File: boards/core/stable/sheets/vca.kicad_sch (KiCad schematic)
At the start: 23 parts, among them Q202 BC847BS, U207 TL072

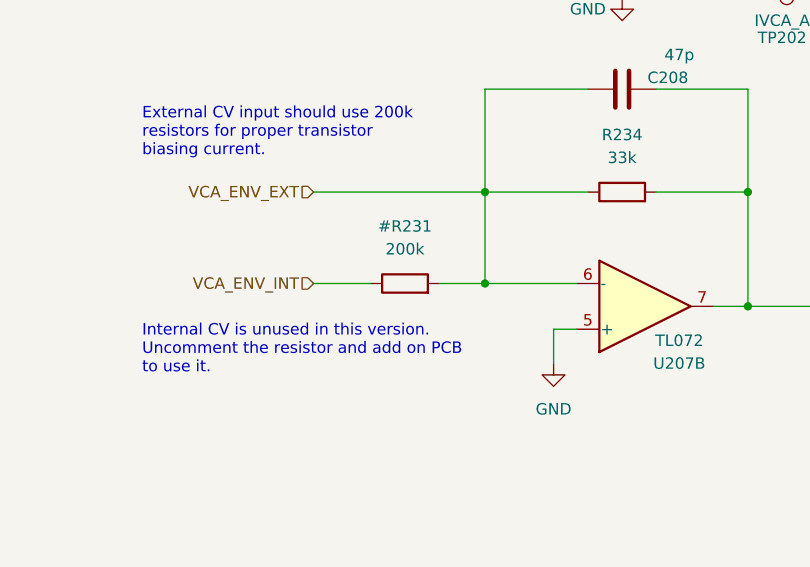
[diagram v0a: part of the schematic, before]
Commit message: Updated and checked Core board BOM
ref https://github.com/shmoergh/hog/issues/19
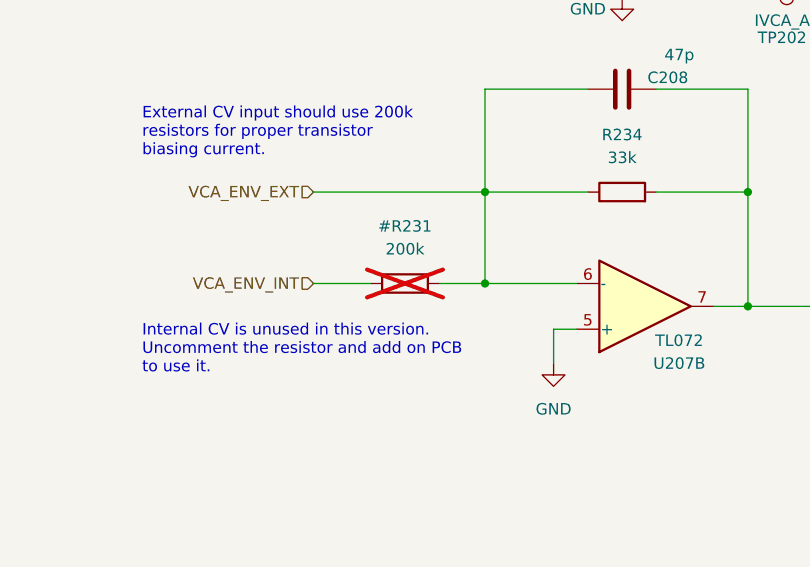
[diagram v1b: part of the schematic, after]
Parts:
- #R231: now not fitted; now left out of the parts list
- C206, C207, C208, R201, R234, R238, R239, R56, R58, R59, U207: Vendor (none) -> JLCPCB
- Q202: LCSC C699265 -> C5380687; Vendor (none) -> JLCPCB
- R54: LCSC (none) -> JLCPCB

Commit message: Added JLCPCB production files to Core
ref https://github.com/shmoergh/hog/issues/19
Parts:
- R54: Field4 C22962 -> (none); LCSC JLCPCB -> C22962; Vendor (none) -> JLCPCB
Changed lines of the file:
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@@
 			)
 		)
-		(property "Field4" "C22962"
+		(property "LCSC" "C22962"
 			(at 130.81 93.98 0)
 			(effects
@@
 			)
 		)
-		(property "Vendor" ""
+		(property "Vendor" "JLCPCB"
 			(at 130.81 93.98 0)
 			(effects
-				(font
-					(size 1.27 1.27)
-				)
-				(hide yes)
-			)
-		)
-		(property "LCSC" "JLCPCB"
-			(at 130.81 93.98 0)
-			(effects

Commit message: Replaced VCA dual BJT footprint
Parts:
- Q202: footprint Package_TO_SOT_SMD:SOT-363_SC-70-6 -> Package_TO_SOT_SMD:SOT-363_SC-70-6_Handsoldering
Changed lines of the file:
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@@
 			)
 		)
-		(property "Footprint" "Package_TO_SOT_SMD:SOT-363_SC-70-6"
+		(property "Footprint" "Package_TO_SOT_SMD:SOT-363_SC-70-6_Handsoldering"
 			(at 154.94 72.39 0)
 			(effects
